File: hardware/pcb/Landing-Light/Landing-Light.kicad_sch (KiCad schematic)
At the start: 49 parts, among them J1 Conn_01x04, J3 USB_C_Receptacle_USB2.0_16P, Q2 NMOS, Q3 NMOS, Q4 PMOS, SW1 SW_SPDT, SW2 SW_SP3T, U1 BQ25172DSGR, U2 SRV05-4, U3 TPS61200DRC

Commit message: Routing complete
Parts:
- removed JP2: Jumper_2_Open, Jumper:SolderJumper-2_P1.3mm_Open_RoundedPad1.0x1.5mm, symbol Jumper:Jumper_2_Open
- added H1, H2: MountingHole, MountingHole:MountingHole_2.2mm_M2, symbol Mechanical:MountingHole
- added R9: 27k, Resistor_SMD:R_0402_1005Metric, symbol Device:R_US
- R10: footprint Resistor_SMD:R_0603_1608Metric -> Resistor_SMD:R_0402_1005Metric; LCSC C22935 -> C26083
- R11: value 180k -> 150k; footprint Resistor_SMD:R_0603_1608Metric -> Resistor_SMD:R_0402_1005Metric; LCSC C22827 -> C25755
- R3: value 180k -> 510k; footprint Resistor_SMD:R_0603_1608Metric -> Resistor_SMD:R_0402_1005Metric; LCSC C22827 -> C11616
- R4: value 470k -> 200k; LCSC C25790 -> C25764
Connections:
- net +5V: now also D6.2 (A)
- net +BATT: now also SW1.1 (A); no longer SW1.2 (B)
- net GND: now also R9.2; no longer R11.2
- net VCC_SW: now also SW1.2 (B); no longer SW1.1 (A)
- new net: R11.2, R9.1
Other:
- moved on the sheet: SW1

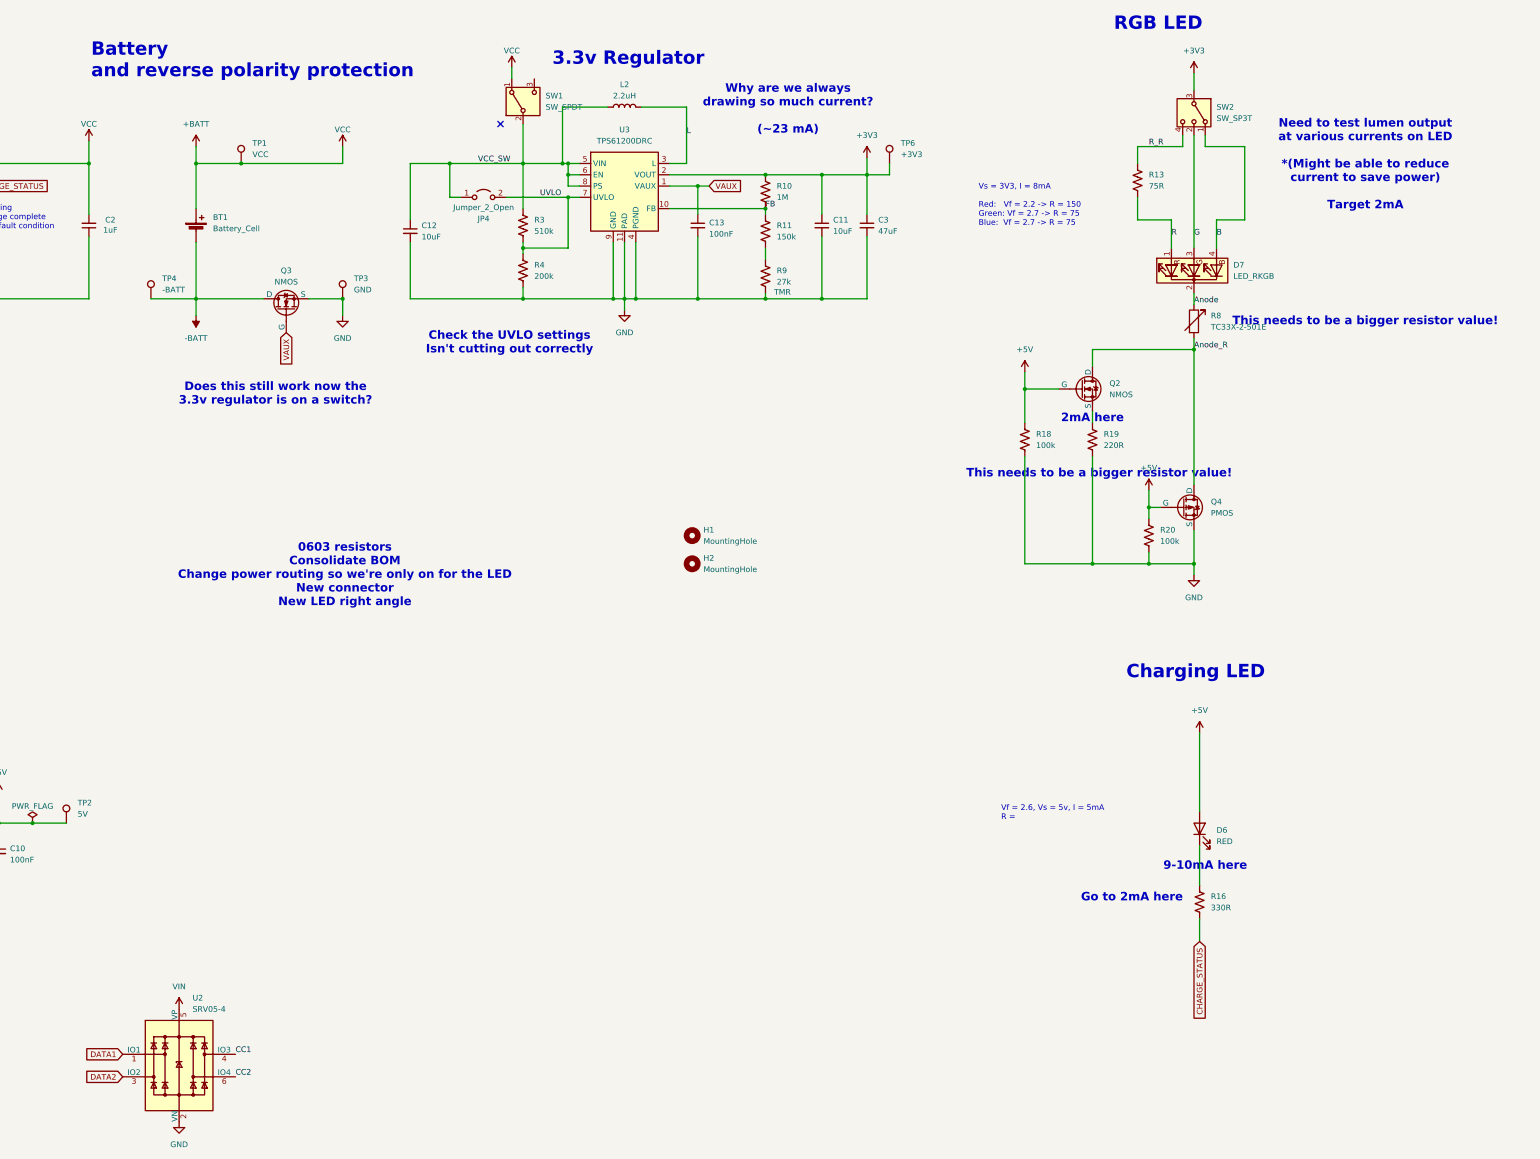
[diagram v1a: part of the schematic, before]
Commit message: Tidying via placement
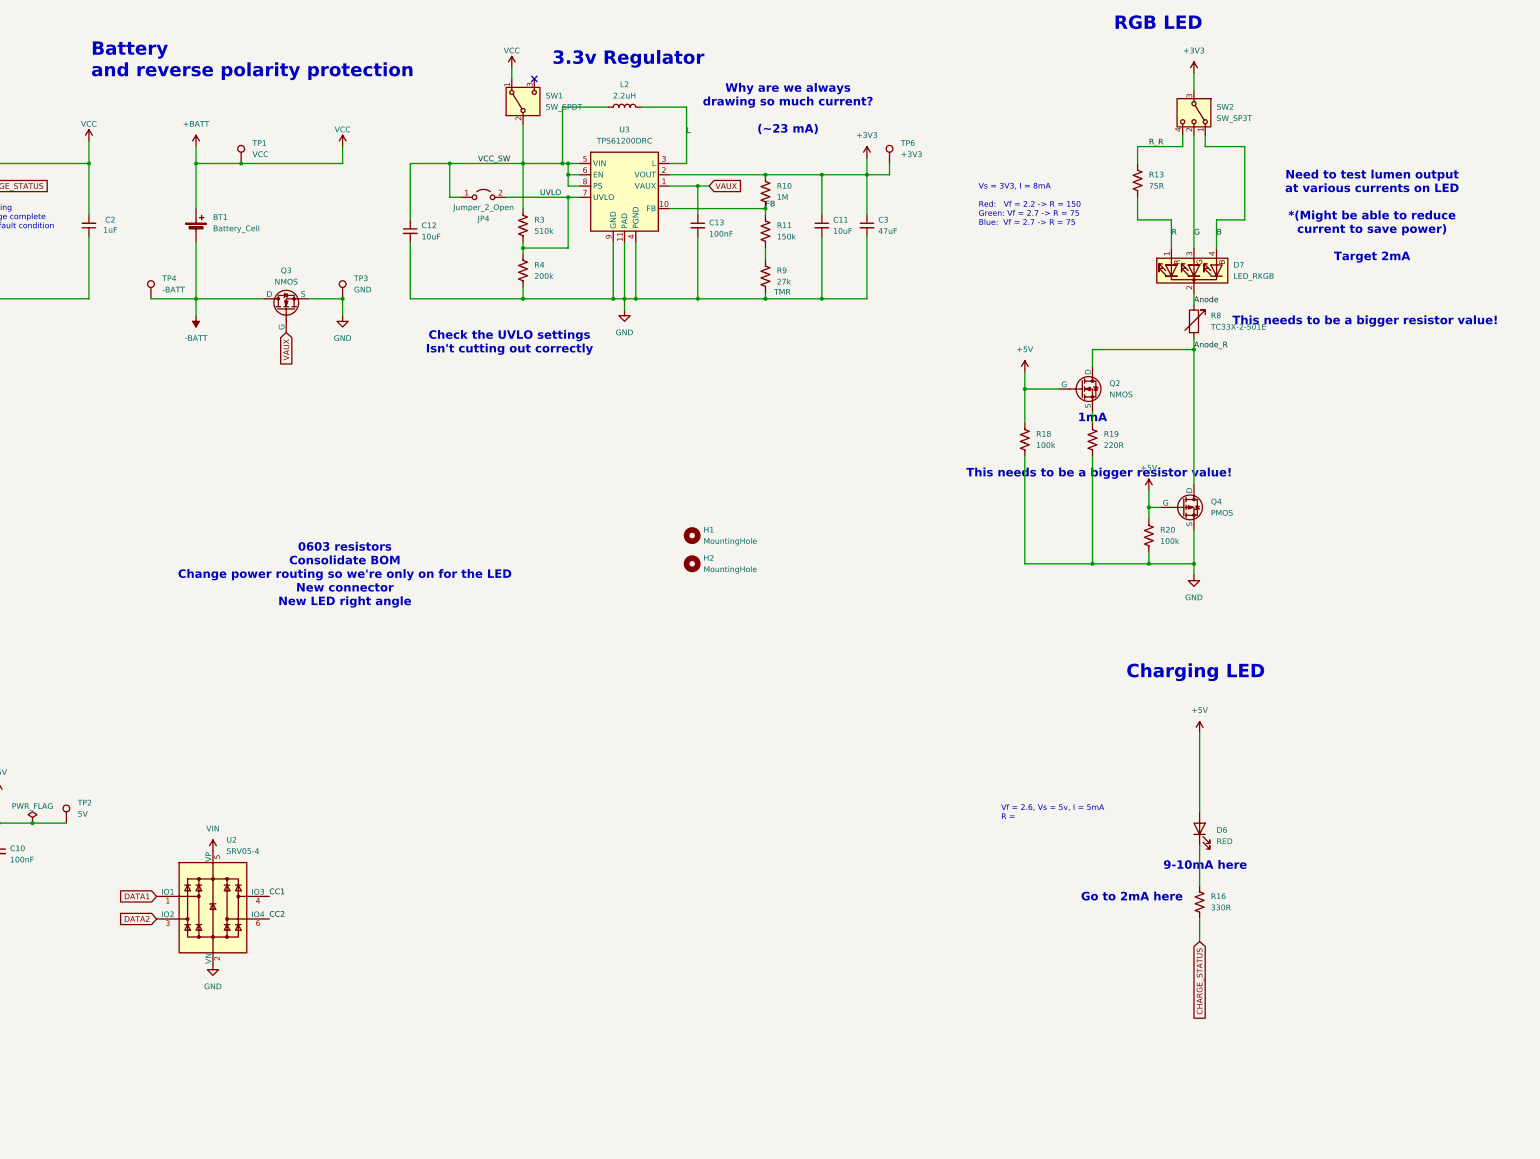
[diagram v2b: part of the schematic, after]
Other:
- note added: "1mA"
- note removed: "2mA here"
- note removed: "Does this still work now the 3.3v regulator is on a switch?"
- moved on the sheet: U2
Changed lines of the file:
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@@
 	(text "Need to test lumen output \nat various currents on LED\n\n*(Might be able to reduce\ncurrent to save power)\n\nTarget 2mA"
 		(exclude_from_sim no)
-		(at 418.338 53.594 0)
+		(at 419.862 65.278 0)
 		(effects
 			(font
@@
 		)
 	)
-	(text "2mA here"
+	(text "1mA"
 		(exclude_from_sim no)
 		(at 356.87 110.744 0)
@@
 		)
 	)
-	(text "Does this still work now the \n3.3v regulator is on a switch?"
-		(exclude_from_sim no)
-		(at 172.8444 105.2592 0)
-		(effects
-			(font
-				(size 1.905 1.905)
-				(thickness 0.381)
-				(bold yes)
-				(color 255 0 0 1)
-			)
-		)
-	)
 	(text "Device Charge Current:\nRiset = 300AOhm / Ichg\n300 / 0.2 = 1.5k"
 		(exclude_from_sim no)
@@
 	)
 	(no_connect
-		(at 223.52 44.45)
+		(at 231.14 34.29)
 	)
 	(no_connect
@@
 	)
 	(label "CC2"
-		(at 163.83 259.08 0)
+		(at 171.45 223.52 0)
 		(effects
 			(font
@@
 	)
 	(label "CC1"
-		(at 163.83 254 0)
+		(at 171.45 218.44 0)
 		(effects
 			(font
@@
 	(global_label "DATA2"
 		(shape input)
-		(at 138.43 259.08 180)
+		(at 146.05 223.52 180)
 		(fields_autoplaced yes)
 		(effects
@@
 		)
 		(property "Intersheetrefs" "${INTERSHEET_REFS}"
-			(at 129.8205 259.08 0)
+			(at 137.4405 223.52 0)
 			(effects
 				(font
@@
 	(global_label "DATA1"
 		(shape input)
-		(at 138.43 254 180)
+		(at 146.05 218.44 180)
 		(fields_autoplaced yes)
 		(effects
@@
 		)
 		(property "Intersheetrefs" "${INTERSHEET_REFS}"
-			(at 129.8205 254 0)
+			(at 137.4405 218.44 0)
 			(effects
 				(font
@@
 	(symbol
 		(lib_id "power:VDC")
-		(at 151.13 243.84 0)
+		(at 158.75 208.28 0)
 		(unit 1)
 		(exclude_from_sim no)
@@
 		(fields_autoplaced yes)
 		(property "Reference" "#PWR015"
-			(at 151.13 247.65 0)
+			(at 158.75 212.09 0)
 			(effects
 				(font
@@
 		)
 		(property "Value" "VIN"
-			(at 151.13 238.76 0)
+			(at 158.75 203.2 0)
 			(effects
 				(font
@@
 		)
 		(property "Footprint" ""
-			(at 151.13 243.84 0)
+			(at 158.75 208.28 0)
 			(effects
 				(font
@@
 		)
 		(property "Datasheet" ""
-			(at 151.13 243.84 0)
+			(at 158.75 208.28 0)
 			(effects
 				(font
@@
 		)
 		(property "Description" "Power symbol creates a global label with name \"VDC\""
-			(at 151.13 243.84 0)
+			(at 158.75 208.28 0)
 			(effects
 				(font
@@
 	(symbol
 		(lib_id "Power_Protection:SRV05-4")
-		(at 151.13 256.54 0)
+		(at 158.75 220.98 0)
 		(unit 1)
 		(exclude_from_sim no)
@@
 		(fields_autoplaced yes)
 		(property "Reference" "U2"
-			(at 154.1465 241.3 0)
+			(at 161.7665 205.74 0)
 			(effects
 				(font
@@
 		)
 		(property "Value" "SRV05-4"
-			(at 154.1465 243.84 0)
+			(at 161.7665 208.28 0)
 			(effects
 				(font
@@
 		)
 		(property "Footprint" "Package_TO_SOT_SMD:SOT-363_SC-70-6"
-			(at 168.91 267.97 0)
+			(at 176.53 232.41 0)
 			(effects
 				(font
@@
 		)
 		(property "Datasheet" "http://www.onsemi.com/pub/Collateral/SRV05-4-D.PDF"
-			(at 151.13 256.54 0)
+			(at 158.75 220.98 0)
 			(effects
 				(font
@@
 		)
 		(property "Description" "ESD Protection Diodes with Low Clamping Voltage, SOT-23-6"
-			(at 151.13 256.54 0)
+			(at 158.75 220.98 0)
 			(effects
 				(font
@@
 		)
 		(property "LCSC" "C15879"
-			(at 151.13 256.54 0)
+			(at 158.75 220.98 0)
 			(effects
 				(font
@@
 	(symbol
 		(lib_id "power:GND")
-		(at 151.13 269.24 0)
+		(at 158.75 233.68 0)
 		(unit 1)
 		(exclude_from_sim no)
@@
 		(fields_autoplaced yes)
 		(property "Reference" "#PWR012"
-			(at 151.13 275.59 0)
+			(at 158.75 240.03 0)
 			(effects
 				(font
@@
 		)
 		(property "Value" "GND"
-			(at 151.13 274.32 0)
+			(at 158.75 238.76 0)
 			(effects
 				(font
@@
 		)
 		(property "Footprint" ""
-			(at 151.13 269.24 0)
+			(at 158.75 233.68 0)
 			(effects
 				(font
@@
 		)
 		(property "Datasheet" ""
-			(at 151.13 269.24 0)
+			(at 158.75 233.68 0)
 			(effects
 				(font
@@
 		)
 		(property "Description" ""
-			(at 151.13 269.24 0)
+			(at 158.75 233.68 0)
 			(effects
 				(font
